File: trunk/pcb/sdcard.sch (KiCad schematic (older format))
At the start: 17 parts, among them P1 SDC_MMC_SOCKET, P2 CONN_8, U1 DS1338-33, X1 32768

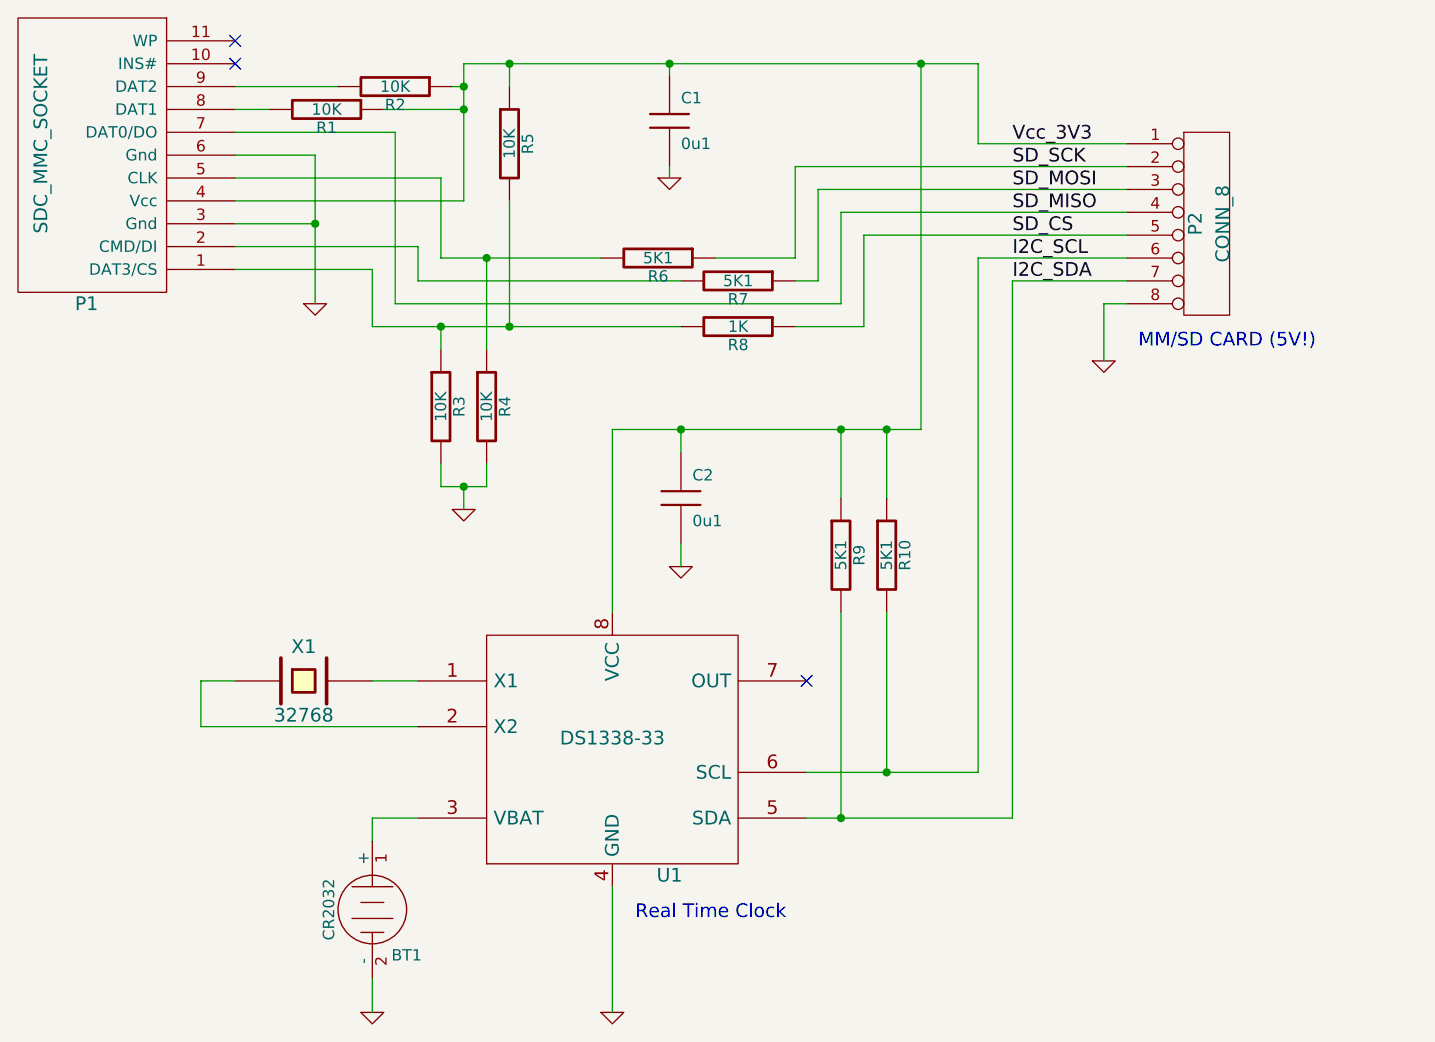
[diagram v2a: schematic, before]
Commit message: SD_CARD schematic correction and SD_CARD PCB design added.
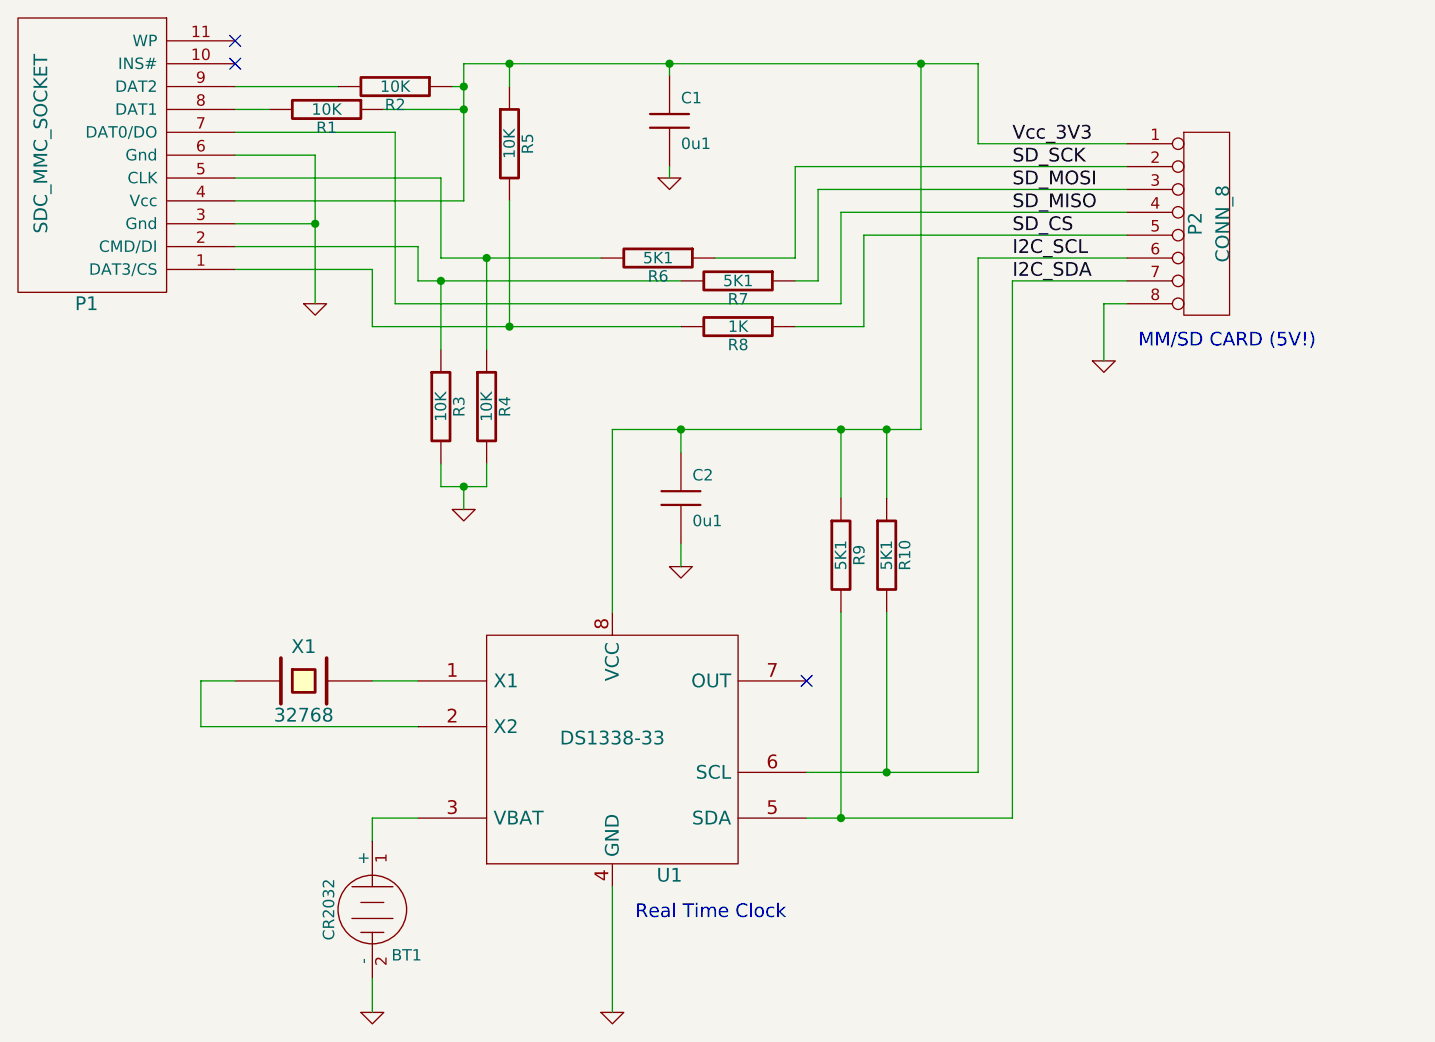
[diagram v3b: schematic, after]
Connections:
- net at P1.2 (CMD/DI), R7.2: now also R3.1
- net at P1.1 (DAT3/CS), R5.2, R8.2: no longer R3.1
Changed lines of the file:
@@
-EESchema Schematic File Version 2  date 25/01/2011 7:11:38 p.m.
+EESchema Schematic File Version 2  date 14/02/2011 9:09:30 p.m.
 LIBS:power
 LIBS:device
@@
 Sheet 1 1
 Title "sdcard.sch"
-Date "25 jan 2011"
+Date "14 feb 2011"
 Rev "3.3"
 Comp ""
@@
 Comment4 ""
 $EndDescr
+Connection ~ 4650 2650
+Wire Wire Line
+	4650 2950 4650 2650
+Connection ~ 6400 5000
+Wire Wire Line
+	6400 4100 6400 5000
+Connection ~ 6600 3300
+Wire Wire Line
+	6600 3600 6600 3300
+Connection ~ 5700 3300
+Wire Wire Line
+	5700 3400 5700 3300
+Connection ~ 6750 1700
+Wire Wire Line
+	6750 1700 6750 3300
+Wire Wire Line
+	6750 3300 5400 3300
+Wire Wire Line
+	5400 3300 5400 4100
+Wire Wire Line
+	4350 5850 4350 5700
+Wire Wire Line
+	4550 4600 3600 4600
+Wire Wire Line
+	3600 4600 3600 4400
+Wire Wire Line
+	3600 4400 3750 4400
+Wire Wire Line
+	7650 2650 7150 2650
+Wire Wire Line
+	7650 2550 7000 2550
+Wire Wire Line
+	7000 2550 7000 4800
+Wire Wire Line
+	7000 4800 6250 4800
+Wire Wire Line
+	4850 3450 4850 3550
+Wire Wire Line
+	4450 2750 6400 2750
+Connection ~ 4950 1700
+Wire Wire Line
+	4950 1700 4950 1800
+Wire Wire Line
+	3750 1800 4200 1800
+Wire Wire Line
+	3750 1900 3900 1900
+Wire Wire Line
+	6200 2850 6500 2850
+Connection ~ 4100 2400
+Wire Wire Line
+	3750 2400 4100 2400
+Wire Wire Line
+	3750 2300 4750 2300
+Wire Wire Line
+	3750 2200 4650 2200
+Wire Wire Line
+	4650 2200 4650 2550
+Wire Wire Line
+	4650 2550 5350 2550
+Wire Wire Line
+	7650 2250 6300 2250
+Wire Wire Line
+	6300 2250 6300 2650
+Wire Wire Line
+	6300 2650 6200 2650
+Wire Wire Line
+	3750 2000 4450 2000
+Wire Wire Line
+	4450 2000 4450 2750
+Wire Wire Line
+	6400 2750 6400 2350
+Wire Wire Line
+	6400 2350 7650 2350
+Wire Wire Line
+	7650 2050 7000 2050
+Wire Wire Line
+	7550 3000 7550 2750
+Wire Wire Line
+	7550 2750 7650 2750
+Wire Wire Line
+	7000 2050 7000 1700
+Wire Wire Line
+	5700 2650 4550 2650
+Wire Wire Line
+	4550 2650 4550 2500
+Wire Wire Line
+	4550 2500 3750 2500
+Wire Wire Line
+	7650 2150 6200 2150
+Wire Wire Line
+	6200 2150 6200 2550
+Wire Wire Line
+	6200 2550 5850 2550
+Wire Wire Line
+	4850 2950 4850 2550
+Connection ~ 4850 2550
+Wire Wire Line
+	4100 2750 4100 2100
+Wire Wire Line
+	4100 2100 3750 2100
+Wire Wire Line
+	5700 2850 4350 2850
+Wire Wire Line
+	4350 2850 4350 2600
+Wire Wire Line
+	4350 2600 3750 2600
+Wire Wire Line
+	5650 2200 5650 2150
+Wire Wire Line
+	4400 1900 4750 1900
+Connection ~ 4750 1900
+Wire Wire Line
+	4750 1800 4700 1800
+Connection ~ 4750 1800
+Wire Wire Line
+	4950 2850 4950 2300
+Connection ~ 4950 2850
+Connection ~ 5650 1700
+Wire Wire Line
+	6500 2850 6500 2450
+Wire Wire Line
+	6500 2450 7650 2450
+Wire Wire Line
+	4750 2300 4750 1700
+Wire Wire Line
+	4750 1700 7000 1700
+Wire Wire Line
+	6250 5000 7150 5000
+Wire Wire Line
+	7150 5000 7150 2650
+Wire Wire Line
+	4550 4400 4350 4400
+Wire Wire Line
+	4350 5100 4350 5000
+Wire Wire Line
+	4350 5000 4550 5000
+Wire Wire Line
+	5400 5850 5400 5300
+Wire Wire Line
+	5700 3900 5700 3800
+Wire Wire Line
+	5650 1700 5650 1750
+Wire Wire Line
+	6400 3300 6400 3600
+Connection ~ 6400 3300
+Wire Wire Line
+	6600 4100 6600 4800
 Connection ~ 6600 4800
 Wire Wire Line
-	6600 4100 6600 4800
-Connection ~ 6400 3300
-Wire Wire Line
-	6400 3600 6400 3300
-Wire Wire Line
-	5650 1700 5650 1750
-Wire Wire Line
-	5700 3900 5700 3800
-Wire Wire Line
-	5400 5850 5400 5300
-Wire Wire Line
-	4550 5000 4350 5000
-Wire Wire Line
-	4350 5000 4350 5100
-Wire Wire Line
-	4550 4400 4350 4400
-Wire Wire Line
-	7150 5000 7150 2650
-Wire Wire Line
-	7150 5000 6400 5000
-Wire Wire Line
-	6400 5000 6250 5000
-Wire Wire Line
-	4750 1700 4950 1700
-Wire Wire Line
-	4950 1700 5650 1700
-Wire Wire Line
-	5650 1700 6750 1700
-Wire Wire Line
-	6750 1700 7000 1700
-Wire Wire Line
-	4750 1700 4750 1800
-Wire Wire Line
-	4750 1800 4750 1900
-Wire Wire Line
-	4750 1900 4750 2300
-Wire Wire Line
-	7650 2450 6500 2450
-Wire Wire Line
-	6500 2450 6500 2850
-Connection ~ 5650 1700
-Connection ~ 4950 2850
-Wire Wire Line
-	4950 2850 4950 2300
-Wire Wire Line
 	4750 3650 4750 3550
-Connection ~ 4750 1800
-Wire Wire Line
-	4750 1800 4700 1800
-Connection ~ 4750 1900
-Wire Wire Line
-	4400 1900 4750 1900
-Wire Wire Line
-	5650 2200 5650 2150
-Connection ~ 4650 2850
-Wire Wire Line
-	4650 2950 4650 2850
-Wire Wire Line
-	3750 2600 4350 2600
-Wire Wire Line
-	4350 2600 4350 2850
-Wire Wire Line
-	4350 2850 4650 2850
-Wire Wire Line
-	4650 2850 4950 2850
-Wire Wire Line
-	4950 2850 5700 2850
-Wire Wire Line
-	3750 2100 4100 2100
-Wire Wire Line
-	4100 2100 4100 2400
-Wire Wire Line
-	4100 2400 4100 2750
-Connection ~ 4850 2550
-Wire Wire Line
-	4850 2950 4850 2550
-Wire Wire Line
-	5850 2550 6200 2550
-Wire Wire Line
-	6200 2550 6200 2150
-Wire Wire Line
-	6200 2150 7650 2150
-Wire Wire Line
-	3750 2500 4550 2500
-Wire Wire Line
-	4550 2500 4550 2650
-Wire Wire Line
-	4550 2650 5700 2650
-Wire Wire Line
-	7000 1700 7000 2050
-Wire Wire Line
-	7650 2750 7550 2750
-Wire Wire Line
-	7550 2750 7550 3000
-Wire Wire Line
-	7000 2050 7650 2050
-Wire Wire Line
-	7650 2350 6400 2350
-Wire Wire Line
-	6400 2350 6400 2750
-Wire Wire Line
-	4450 2000 4450 2750
-Wire Wire Line
-	4450 2000 3750 2000
-Wire Wire Line
-	6200 2650 6300 2650
-Wire Wire Line
-	6300 2650 6300 2250
-Wire Wire Line
-	6300 2250 7650 2250
-Wire Wire Line
-	5350 2550 4850 2550
-Wire Wire Line
-	4850 2550 4650 2550
-Wire Wire Line
-	4650 2550 4650 2200
-Wire Wire Line
-	4650 2200 3750 2200
-Wire Wire Line
-	4750 2300 3750 2300
-Wire Wire Line
-	3750 2400 4100 2400
-Connection ~ 4100 2400
-Wire Wire Line
-	6500 2850 6200 2850
-Wire Wire Line
-	4650 3450 4650 3550
-Wire Wire Line
-	3750 1900 3900 1900
-Wire Wire Line
-	3750 1800 4200 1800
-Wire Wire Line
-	4950 1700 4950 1800
-Connection ~ 4950 1700
-Wire Wire Line
-	4450 2750 6400 2750
-Wire Wire Line
-	4650 3550 4750 3550
-Wire Wire Line
-	4750 3550 4850 3550
-Wire Wire Line
-	4850 3550 4850 3450
 Connection ~ 4750 3550
 Wire Wire Line
-	6250 4800 6600 4800
-Wire Wire Line
-	6600 4800 7000 4800
-Wire Wire Line
-	7000 4800 7000 2550
-Wire Wire Line
-	7000 2550 7650 2550
-Wire Wire Line
-	7150 2650 7650 2650
-Wire Wire Line
-	3750 4400 3600 4400
-Wire Wire Line
-	3600 4400 3600 4600
-Wire Wire Line
-	3600 4600 4550 4600
-Wire Wire Line
-	4350 5850 4350 5700
-Wire Wire Line
-	5400 4100 5400 3300
-Wire Wire Line
-	5400 3300 5700 3300
-Wire Wire Line
-	5700 3300 6400 3300
-Wire Wire Line
-	6400 3300 6600 3300
-Wire Wire Line
-	6600 3300 6750 3300
-Wire Wire Line
-	6750 3300 6750 1700
-Connection ~ 6750 1700
-Wire Wire Line
-	5700 3400 5700 3300
-Connection ~ 5700 3300
-Wire Wire Line
-	6600 3600 6600 3300
-Connection ~ 6600 3300
-Wire Wire Line
-	6400 4100 6400 5000
-Connection ~ 6400 5000
+	4850 3550 4650 3550
+Wire Wire Line
+	4650 3550 4650 3450
+$Comp
+L R R3
+U 1 1 4D1F93EA
+P 4650 3200
+F 0 "R3" V 4730 3200 50  0000 C CNN
+F 1 "10K" V 4650 3200 50  0000 C CNN
+	1    4650 3200
+	1    0    0    -1
+$EndComp
 $Comp
 L R R10
@@
 Real Time Clock
 $Comp
-L GND #PWR6
+L GND #PWR01
 U 1 1 4D3E3F0B
 P 5700 3900
-F 0 "#PWR6" H 5700 3900 30  0001 C CNN
+F 0 "#PWR01" H 5700 3900 30  0001 C CNN
 F 1 "GND" H 5700 3830 30  0001 C CNN
 	1    5700 3900
@@
 $EndComp
 $Comp
-L GND #PWR2
+L GND #PWR02
 U 1 1 4D3E3EC2
 P 4350 5850
-F 0 "#PWR2" H 4350 5850 30  0001 C CNN
+F 0 "#PWR02" H 4350 5850 30  0001 C CNN
 F 1 "GND" H 4350 5780 30  0001 C CNN
 	1    4350 5850
@@
 $EndComp
 $Comp
-L GND #PWR4
+L GND #PWR03
 U 1 1 4D3E3EBC
 P 5400 5850
-F 0 "#PWR4" H 5400 5850 30  0001 C CNN
+F 0 "#PWR03" H 5400 5850 30  0001 C CNN
 F 1 "GND" H 5400 5780 30  0001 C CNN
 	1    5400 5850
@@
 $EndComp
 $Comp
-L GND #PWR5
+L GND #PWR04
 U 1 1 4D1F9457
 P 5650 2200
-F 0 "#PWR5" H 5650 2200 30  0001 C CNN
+F 0 "#PWR04" H 5650 2200 30  0001 C CNN
 F 1 "GND" H 5650 2130 30  0001 C CNN
 	1    5650 2200
@@
 $EndComp
 $Comp
-L R R3
-U 1 1 4D1F93EA
-P 4650 3200
-F 0 "R3" V 4730 3200 50  0000 C CNN
-F 1 "10K" V 4650 3200 50  0000 C CNN
-	1    4650 3200
-	1    0    0    -1
-$EndComp
-$Comp
 L R R8
 U 1 1 4D1F93CC
@@
 $EndComp
 $Comp
-L GND #PWR3
+L GND #PWR05
 U 1 1 4D1F93AF
 P 4750 3650
-F 0 "#PWR3" H 4750 3650 30  0001 C CNN
+F 0 "#PWR05" H 4750 3650 30  0001 C CNN
 F 1 "GND" H 4750 3580 30  0001 C CNN
 	1    4750 3650
@@
 $EndComp
 $Comp
-L GND #PWR1
+L GND #PWR06
 U 1 1 4D1F938F
 P 4100 2750
-F 0 "#PWR1" H 4100 2750 30  0001 C CNN
+F 0 "#PWR06" H 4100 2750 30  0001 C CNN
 F 1 "GND" H 4100 2680 30  0001 C CNN
 	1    4100 2750
@@
 $EndComp
 $Comp
-L GND #PWR7
+L GND #PWR07
 U 1 1 4D1F869F
 P 7550 3000
-F 0 "#PWR7" H 7550 3000 30  0001 C CNN
+F 0 "#PWR07" H 7550 3000 30  0001 C CNN
 F 1 "GND" H 7550 2930 30  0001 C CNN
 	1    7550 3000
